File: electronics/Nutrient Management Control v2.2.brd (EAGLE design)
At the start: 101.6 x 81.3 mm, 14 parts, among them IC1 7407N, Q1 FQP30N06L

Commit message: Correcting pins, debug and naming conventions
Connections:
- removed net RT_DSO: PCB2.27, RT_DS.4
- new net IST_DSMS: IST_DS.3, PCB2.47
- new net RRT_DSMS: PCB2.49, RT_DS.3
- new net RRT_DSO: PCB2.53, RT_DS.4
- net +5V: no longer IST_DS.3, RT_DS.3
- net IST_DSO: now also PCB2.51; no longer PCB2.25
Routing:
- net RT_DSO: track 52.5 -> 0.00 mm
- net RRT_DSO: track 0.00 -> 52.4 mm
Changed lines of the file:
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@@
 <drawing>
 <settings>
-<setting alwaysvectorfont="no"/>
+<setting alwaysvectorfont="yes"/>
 <setting verticaltext="up"/>
 </settings>
@@
 <contactref element="IST_DS" pad="1"/>
 <contactref element="RT_DS" pad="1"/>
-<contactref element="IST_DS" pad="3"/>
-<contactref element="RT_DS" pad="3"/>
 <wire x1="6.4008" y1="57.4548" x2="6.4008" y2="55.9308" width="0.508" layer="1"/>
 <wire x1="13.716" y1="64.77" x2="6.4008" y2="57.4548" width="0.508" layer="1"/>
@@
 <wire x1="79.3242" y1="11.3538" x2="77.9526" y2="11.3538" width="0.508" layer="1"/>
 <wire x1="80.4672" y1="10.2108" x2="79.3242" y2="11.3538" width="0.508" layer="1"/>
-<wire x1="76.5048" y1="10.2108" x2="76.47" y2="10.16" width="0.508" layer="1"/>
 <wire x1="80.4672" y1="10.2108" x2="80.47" y2="10.16" width="0.508" layer="1"/>
 <wire x1="88.2396" y1="10.2108" x2="87.9348" y2="10.2108" width="0.508" layer="1"/>
@@
 <wire x1="90.7542" y1="11.3538" x2="89.3826" y2="11.3538" width="0.508" layer="1"/>
 <wire x1="91.8972" y1="10.2108" x2="90.7542" y2="11.3538" width="0.508" layer="1"/>
-<wire x1="87.9348" y1="10.2108" x2="87.9" y2="10.16" width="0.508" layer="1"/>
 <wire x1="91.8972" y1="10.2108" x2="91.9" y2="10.16" width="0.508" layer="1"/>
 <wire x1="84.2772" y1="10.2108" x2="80.5434" y2="10.2108" width="0.508" layer="16"/>
@@
 <wire x1="87.8586" y1="10.2108" x2="86.7156" y2="11.3538" width="0.508" layer="16"/>
 <wire x1="80.5434" y1="10.2108" x2="80.47" y2="10.16" width="0.508" layer="16"/>
-<wire x1="87.8586" y1="10.2108" x2="87.9" y2="10.16" width="0.508" layer="16"/>
 <wire x1="17.7546" y1="41.91" x2="15.24" y2="41.91" width="0.508" layer="1"/>
 <wire x1="25.3746" y1="49.53" x2="17.7546" y2="41.91" width="0.508" layer="1"/>
@@
 <wire x1="37.0332" y1="15.0114" x2="71.3232" y2="15.0114" width="0.508" layer="16"/>
 <wire x1="35.5854" y1="16.4592" x2="37.0332" y2="15.0114" width="0.508" layer="16"/>
-<wire x1="76.4286" y1="10.2108" x2="76.47" y2="10.16" width="0.508" layer="16"/>
 <wire x1="35.5854" y1="16.4592" x2="35.56" y2="16.51" width="0.508" layer="16"/>
 <wire x1="6.4008" y1="55.626" x2="6.4008" y2="55.8546" width="0.508" layer="16"/>
@@
 <wire x1="15.24" y1="41.91" x2="12.8016" y2="44.3484" width="0.508" layer="16"/>
 <wire x1="6.4008" y1="55.8546" x2="6.35" y2="55.88" width="0.508" layer="16"/>
+<wire x1="87.8586" y1="10.2108" x2="87.9348" y2="10.2108" width="0" layer="19" extent="1-16"/>
+<wire x1="76.4286" y1="10.2108" x2="76.5048" y2="10.2108" width="0" layer="19" extent="1-16"/>
 </signal>
 <signal name="+12V" class="4">
@@
 <signal name="IST_DSO">
 <contactref element="IST_DS" pad="4"/>
-<contactref element="PCB2" pad="25"/>
 <wire x1="85.9536" y1="12.2682" x2="85.9536" y2="10.2108" width="0.1524" layer="1"/>
 <wire x1="89.0778" y1="15.3924" x2="85.9536" y2="12.2682" width="0.1524" layer="1"/>
@@
 <wire x1="86.4108" y1="59.6646" x2="89.0778" y2="56.9976" width="0.1524" layer="1"/>
 <wire x1="85.9536" y1="10.2108" x2="85.9" y2="10.16" width="0.1524" layer="1"/>
-<wire x1="86.4108" y1="59.6646" x2="86.36" y2="59.69" width="0.1524" layer="1"/>
-</signal>
-<signal name="RT_DSO">
+<contactref element="PCB2" pad="51"/>
+<wire x1="85.9" y1="10.16" x2="86.36" y2="26.67" width="0" layer="19" extent="1-1"/>
+</signal>
+<signal name="RRT_DSO">
 <contactref element="RT_DS" pad="4"/>
-<contactref element="PCB2" pad="27"/>
 <wire x1="74.5236" y1="10.5918" x2="74.5236" y2="10.2108" width="0.1524" layer="1"/>
 <wire x1="80.0862" y1="16.1544" x2="74.5236" y2="10.5918" width="0.1524" layer="1"/>
@@
 <wire x1="86.3346" y1="57.15" x2="85.1916" y2="56.007" width="0.1524" layer="1"/>
 <wire x1="74.5236" y1="10.2108" x2="74.47" y2="10.16" width="0.1524" layer="1"/>
-<wire x1="86.3346" y1="57.15" x2="86.36" y2="57.15" width="0.1524" layer="1"/>
+<contactref element="PCB2" pad="53"/>
+<wire x1="74.47" y1="10.16" x2="86.36" y2="24.13" width="0" layer="19" extent="1-1"/>
+</signal>
+<signal name="IST_DSMS">
+<contactref element="IST_DS" pad="3"/>
+<contactref element="PCB2" pad="47"/>
+<wire x1="87.9" y1="10.16" x2="86.36" y2="31.75" width="0" layer="19" extent="1-1"/>
+</signal>
+<signal name="RRT_DSMS">
+<contactref element="RT_DS" pad="3"/>
+<contactref element="PCB2" pad="49"/>
+<wire x1="76.47" y1="10.16" x2="86.36" y2="29.21" width="0" layer="19" extent="1-1"/>
 </signal>
 </signals>

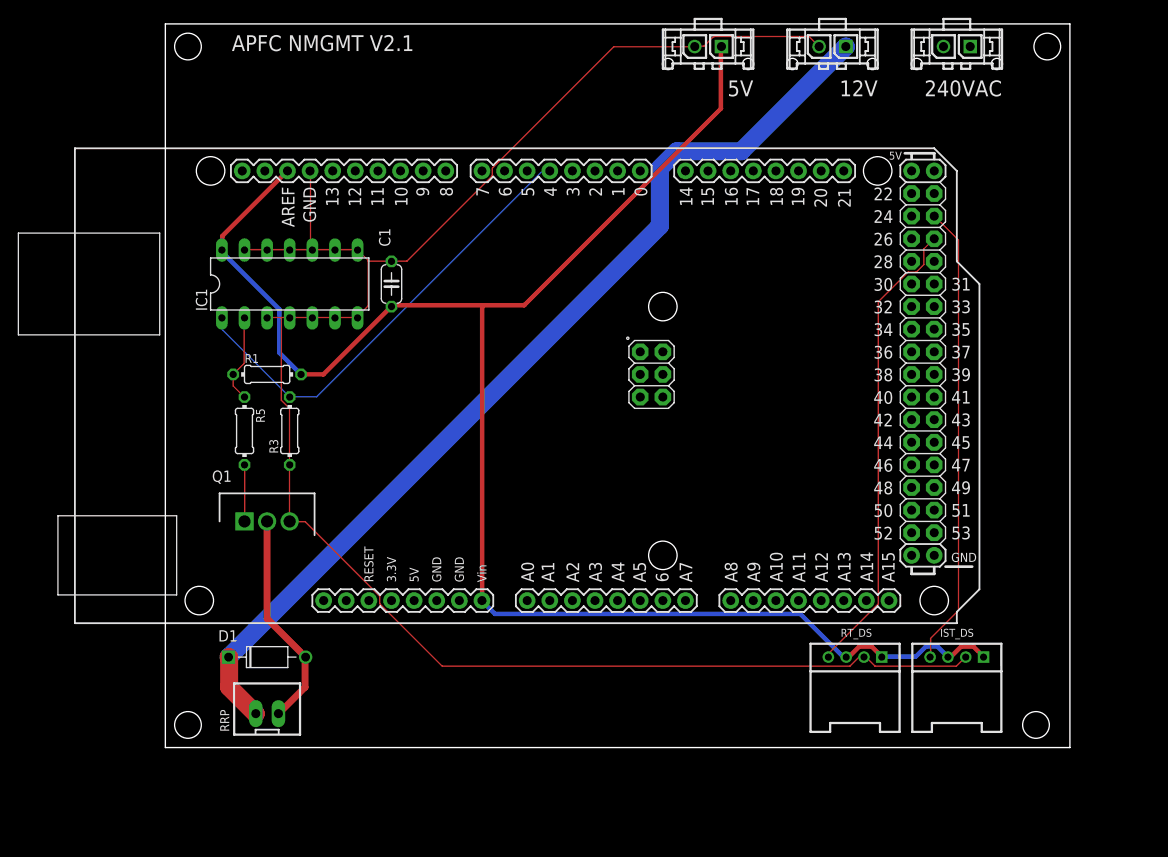
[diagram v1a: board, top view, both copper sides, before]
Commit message: First cut of Nutrient Management with multi UART breakout boards
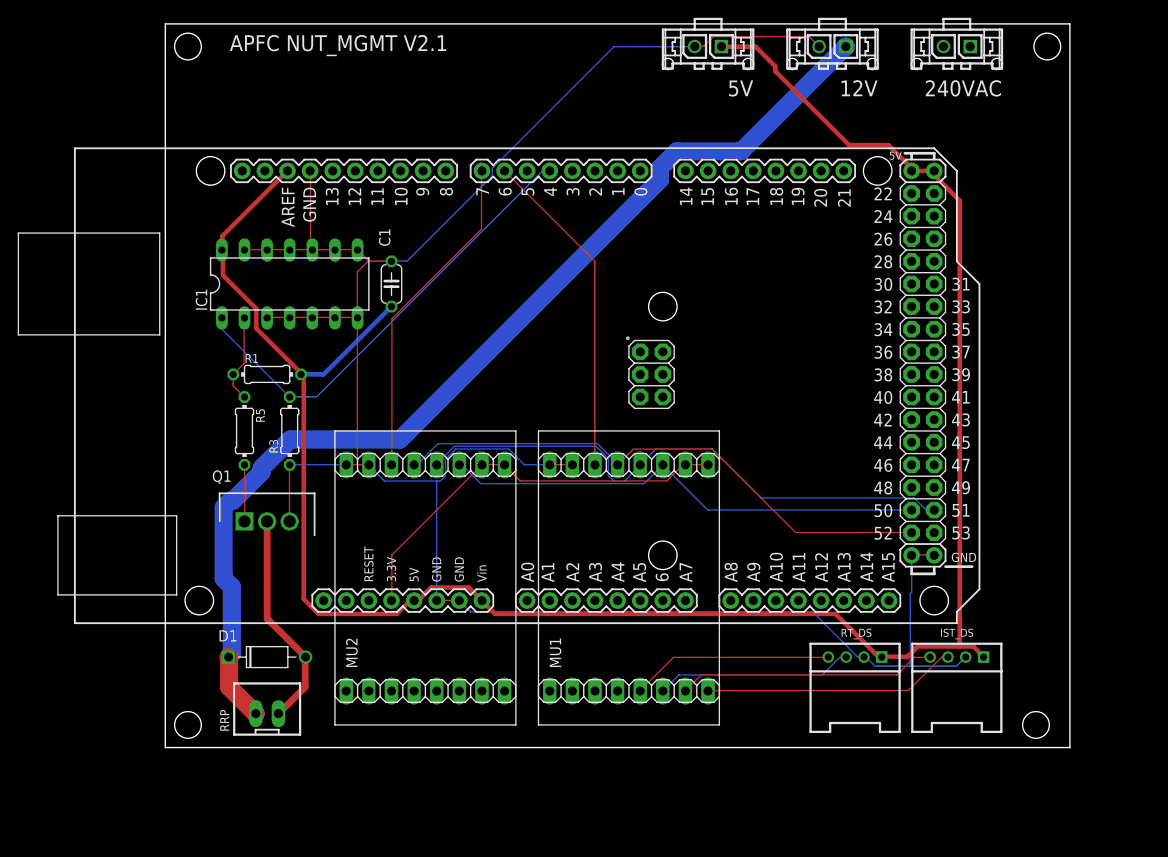
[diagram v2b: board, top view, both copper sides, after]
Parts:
- added MU1, MU2: SPI2UART_HEADERS, Aeroponics Control:SPI2UARTV2
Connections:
- new net +3V3: MU1.10, MU1.9, MU2.10, MU2.9, PCB2.3.3V
- new net CIPO: MU1.11, MU2.11, PCB2.50
- new net COPI: MU1.12, MU2.12, PCB2.51
- new net MU1CS: MU1.14, PCB2.6
- new net MU2CS: MU2.14, PCB2.7
- new net SCK: MU1.13, MU2.13, PCB2.52
- net +5V: now also PCB2.5V, PCB2.5V., PCB2.5V..
- net GND: now also MU1.15, MU1.16, MU2.15, MU2.16, PCB2.GND., PCB2.GND.., PCB2.GND..., PCB2.GND....
- net IST_DSMS: now also MU1.1; no longer PCB2.47
- net IST_DSO: now also MU1.2; no longer PCB2.51
- net RRT_DSMS: now also MU1.3; no longer PCB2.49
- net RRT_DSO: now also MU1.4; no longer PCB2.53
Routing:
- net COPI: track 0.00 -> 63.9 mm
- net SCK: track 0.00 -> 62.6 mm
- net CIPO: track 0.00 -> 54.7 mm
- net +3V3: track 0.00 -> 46.5 mm
- net +5V: track 191.1 -> 235.5 mm
- net GND: track 211.0 -> 253.6 mm
- net MU2CS: track 0.00 -> 37.3 mm
- net MU1CS: track 0.00 -> 37.2 mm
- net RRT_DSO: track 52.4 -> 22.7 mm
- net IST_DSMS: track 0.00 -> 28.5 mm
- net IST_DSO: track 51.9 -> 29.1 mm
- net RRT_DSMS: track 0.00 -> 22.2 mm
- net +12V: track 109.2 -> 117.3 mm
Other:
- board text added: "APFC NUT_MGMT V2.1"
- board text removed: "APFC NMGMT V2.1"

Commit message: Added UV Steriliser
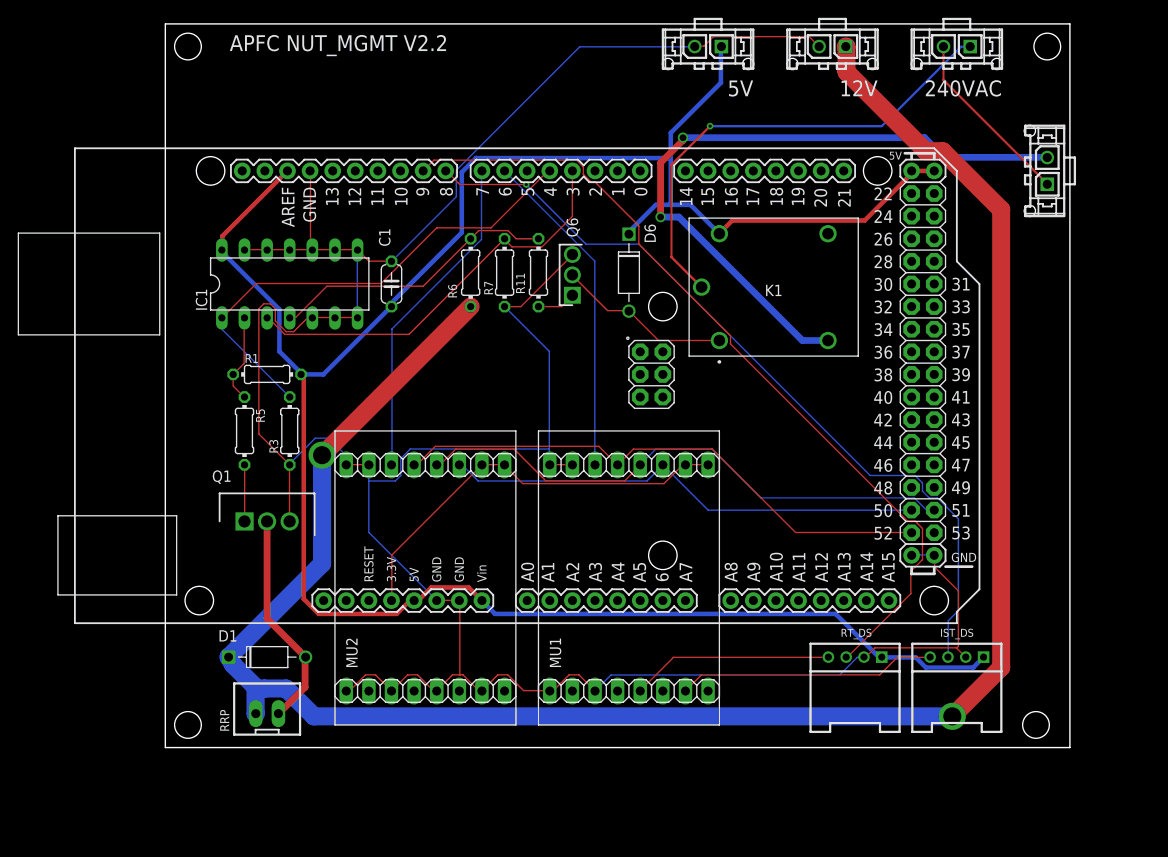
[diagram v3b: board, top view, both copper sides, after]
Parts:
- added D6: 1N4004, Aeroponics Control:DO-41
- added K1: SRM-1C-SL-5VDC, Aeroponics Control:SRM1CSL5VDC
- added Q6: FDU3N40TU, Aeroponics Control:TO229P250X658X985-3P
- added R11: 1K, Aeroponics Control:0204/7
- added R6: 10k, Aeroponics Control:0204/7
- added R7: 1k, Aeroponics Control:0204/7
- added UVCTL: UVCTL, Aeroponics Control:43650-0215
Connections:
- new net N$13: Q6.1, R11.2
- new net N$17: IC1.4, R11.1, R6.1
- new net N$21: D6.A, K1.1, Q6.2
- new net N$7: K1.2, UVCTL.P$2
- new net UVCTL: IC1.3, PCB2.3, R7.2
- net +12V: now also R6.2
- net +240VAC: now also K1.5
- net +5V: now also D6.C, K1.4
- net -240VAC: now also UVCTL.P$1
- net GND: now also MU1.6, MU1.8, MU2.2, MU2.4, MU2.6, MU2.8, Q6.3, R7.1; no longer IC1.3, IC1.4
- net IST_DSMS: now also PCB2.8; no longer MU1.1
- net RRT_DSMS: now also PCB2.9; no longer MU1.3
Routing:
- net +12V: track 117.3 -> 223.6 mm, vias 0 -> 2
- net N$7: track 0.00 -> 76.4 mm, vias 0 -> 2
- net RRT_DSMS: track 22.2 -> 94.0 mm
- net GND: track 253.6 -> 325.1 mm
- net IST_DSMS: track 28.5 -> 90.3 mm, vias 0 -> 1
- net +240VAC: track 0.00 -> 54.2 mm, vias 0 -> 1
- net UVCTL: track 0.00 -> 46.5 mm
- net N$17: track 0.00 -> 32.4 mm
- net -240VAC: track 0.00 -> 20.3 mm
- net N$21: track 0.00 -> 19.6 mm
- net +5V: track 235.5 -> 253.6 mm
- net N$13: track 0.00 -> 4.37 mm
- net RRPCTL: track 51.8 -> 55.7 mm
- net COPI: track 63.9 -> 62.5 mm
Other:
- board text added: "APFC NUT_MGMT V2.2"
- board text removed: "APFC NUT_MGMT V2.1"

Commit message: Sorting out Nutrient Control Electronics
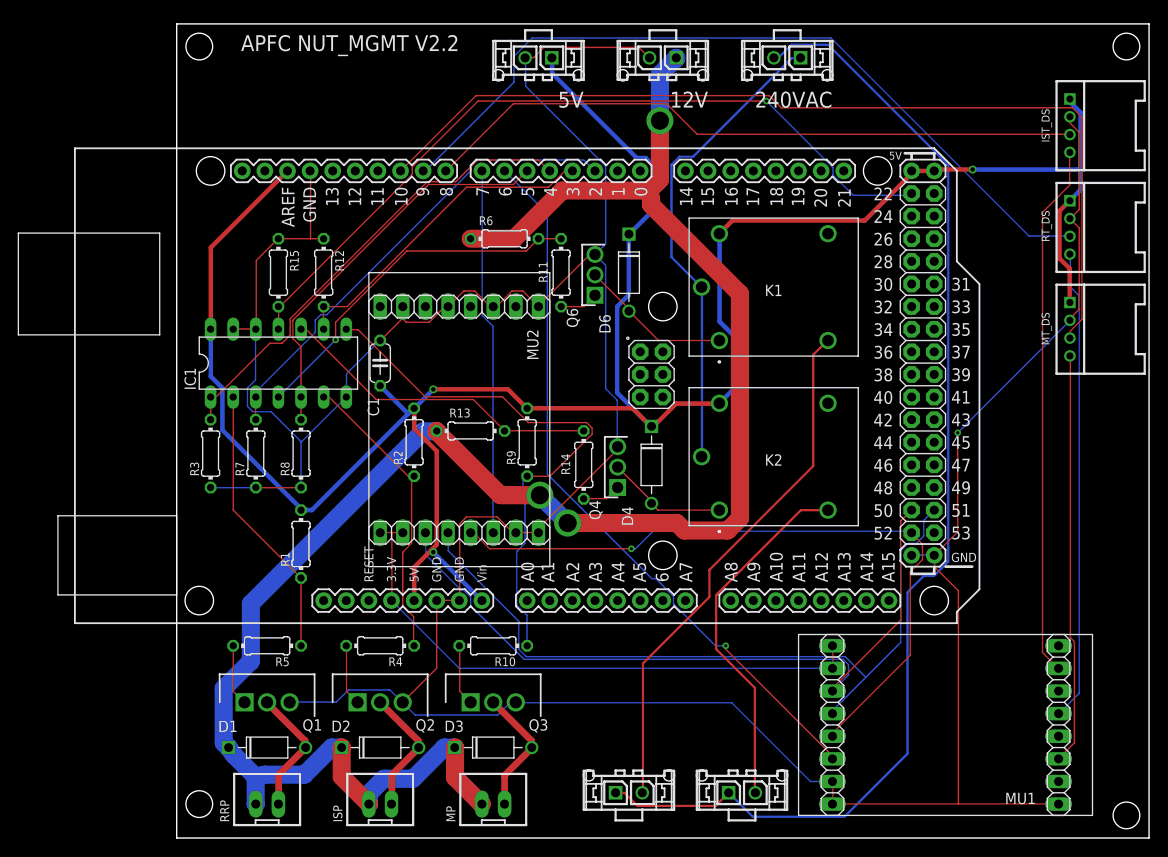
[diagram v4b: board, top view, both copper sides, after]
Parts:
- added D2, D3, D4: 1N4004, Aeroponics Control:DO-41
- added HCTL: (no value), Aeroponics Control:43650-0215
- added ISP, MP: JST-XH-02-PIN-LONG-PAD, Aeroponics Control:JST-XH-02-PACKAGE-LONG-PAD
- added K2: SRM-1C-SL-5VDC, Aeroponics Control:SRM1CSL5VDC
- added MT_DS: 4P-2.0-90D, Aeroponics Control:HW4-2.0-90D
- added Q2, Q3: FQP30N06L, Aeroponics Control:TO254P470X1016X2019-3P
- added Q4: FDU3N40TU, Aeroponics Control:TO229P250X658X985-3P
- added R10, R14, R4: 1K, Aeroponics Control:0204/7
- added R12, R15, R8: 1k, Aeroponics Control:0204/7
- added R13, R2, R9: 10k, Aeroponics Control:0204/7
- UVCTL: value UVCTL -> (none)
- moved UVCTL 84.2 mm to (52.1, -5.08), turned to 180 degrees
- moved IST_DS 61.0 mm to (101.6, 69.8), turned to 270 degrees
- moved RT_DS 54.0 mm to (101.6, 58.4), turned to 270 degrees
- moved MU1 39.2 mm to (87.6, 2.54), turned to 180 degrees
- moved R7 34.5 mm to (10.2, 33.0)
- moved R5 24.3 mm to (11.4, 11.4), turned to 180 degrees
- moved Q1 20.3 mm to (8.89, 5.08)
- moved R1 19.4 mm to (15.2, 22.9), turned to 90 degrees
- moved 240ACVS 19.1 mm to (69.8, 77.5)
- moved 12VS 19.1 mm to (55.9, 77.5)
- moved 5VS 19.1 mm to (41.9, 77.5)
- moved MU2 18.2 mm to (33.0, 36.8), turned to 270 degrees
- moved D1 10.2 mm to (11.4, 0.00)
- moved RRP 10.2 mm to (11.4, -6.35)
- moved R3 9.25 mm to (5.08, 33.0)
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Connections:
- new net HCTL: IC1.11, PCB2.22, R15.2
- new net ISPCTL: IC1.5, PCB2.5, R8.2
- new net MPCTL: IC1.9, PCB2.3, R12.2
- new net MT_DSMS: MT_DS.3, PCB2.10
- new net N$1: D2.A, ISP.2, Q2.2
- new net N$11: MT_DS.4, MU1.6
- new net N$12: D4.A, K2.1, Q4.2
- new net N$14: HCTL.P$2, K2.2
- new net N$15: Q4.1, R14.2
- new net N$16: IC1.10, R13.1, R14.1
- new net N$2: IC1.6, R2.1, R4.1
- new net N$4: Q2.1, R4.2
- new net N$6: D3.A, MP.2, Q3.2
- new net N$8: IC1.8, R10.1, R9.1
- new net N$9: Q3.1, R10.2
- net +12V: now also D2.C, D3.C, ISP.1, MP.1, R13.2
- net +240VAC: now also K2.5
- net +5V: now also D4.C, K2.4, MT_DS.1, R2.2, R9.2
- net -240VAC: now also HCTL.P$1
- net GND: now also MT_DS.2, Q2.3, Q3.3, Q4.3, R12.1, R15.1, R8.1; no longer IC1.10, IC1.11, IC1.5, IC1.6, IC1.8, IC1.9, MU1.6
- net UVCTL: now also PCB2.2; no longer PCB2.3
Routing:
- net -240VAC: track 20.3 -> 132.6 mm
- net MT_DSMS: track 0.00 -> 106.4 mm
- net HCTL: track 0.00 -> 88.7 mm, vias 0 -> 1
- net GND: track 325.1 -> 403.4 mm, vias 0 -> 1
- net N$8: track 0.00 -> 62.4 mm
- net N$11: track 0.00 -> 46.2 mm
- net MU1CS: track 37.2 -> 82.2 mm, vias 0 -> 1
- net ISPCTL: track 0.00 -> 44.8 mm
- net N$14: track 0.00 -> 40.5 mm
- net MPCTL: track 0.00 -> 36.8 mm
- net N$16: track 0.00 -> 36.6 mm
- net N$2: track 0.00 -> 34.1 mm
- net IST_DSO: track 29.1 -> 60.0 mm
- net RRT_DSO: track 22.7 -> 53.0 mm
- net CIPO: track 54.4 -> 83.4 mm
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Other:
- board size 101.6 x 81.3 mm -> 109.2 x 91.4 mm
